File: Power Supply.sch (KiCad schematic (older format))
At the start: 24 parts

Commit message: Added all submoduels
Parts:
- added D?: LED, symbol LED
- added SW?: SPST, symbol SPST
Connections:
- net Earth: no longer R?.2
- net GND: now also D?.2 (A)
- net at D?.2, P?.2 (P2), SW?.1: now also R?.2
- net at F?.2, SW?.5: now also SW?.1
- net at D?.2 (A): now also D?.1 (K); no longer R?.1
- new net Voltage Multiplier/VAC+: SW?.2
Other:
- moved on the sheet: R?
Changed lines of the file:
@@
 LIBS:contrib
 LIBS:valves
-LIBS:switch_dpdt
-LIBS:switch_spdt
 LIBS:Power Supply-cache
 EELAYER 25 0
@@
 $Descr A4 11693 8268
 encoding utf-8
-Sheet 1 1
+Sheet 1 5
 Title "Power Supply"
 Date ""
@@
 L R R?
 U 1 1 55CE60EE
-P 4450 4650
-F 0 "R?" V 4530 4650 50  0000 C CNN
-F 1 "R" V 4450 4650 50  0000 C CNN
-F 2 "" V 4380 4650 30  0000 C CNN
-F 3 "" H 4450 4650 30  0000 C CNN
-	1    4450 4650
-	1    0    0    -1
-$EndComp
-$Comp
-L Earth #PWR?
-U 1 1 55CE6153
-P 4450 4800
-F 0 "#PWR?" H 4450 4550 50  0001 C CNN
-F 1 "Earth" H 4450 4650 50  0001 C CNN
-F 2 "" H 4450 4800 60  0000 C CNN
-F 3 "" H 4450 4800 60  0000 C CNN
-	1    4450 4800
+P 4600 4650
+F 0 "R?" V 4680 4650 50  0000 C CNN
+F 1 "R" V 4600 4650 50  0000 C CNN
+F 2 "" V 4530 4650 30  0000 C CNN
+F 3 "" H 4600 4650 30  0000 C CNN
+	1    4600 4650
 	1    0    0    -1
 $EndComp
@@
 	1    0    0    -1
 $EndComp
+$Sheet
+S 5400 900  1400 1450
+U 564515C4
+F0 "Voltage Multiplier" 60
+F1 "Voltage Multiplier.sch" 60
+F2 "VAC+" I L 5400 1200 60
+F3 "VAC-" I L 5400 1950 60
+F4 "5xVDC" I R 6800 1950 60
+$EndSheet
+$Sheet
+S 9400 4200 1200 1450
+U 564650FF
+F0 "Timer" 60
+F1 "Timer.sch" 60
+$EndSheet
+$Sheet
+S 8250 900  1150 1500
+U 56465396
+F0 "Signal Amplifier" 60
+F1 "Signal Amplifier.sch" 60
+$EndSheet
+$Comp
+L Earth #PWR?
+U 1 1 56468113
+P 5200 2000
+F 0 "#PWR?" H 5200 1750 50  0001 C CNN
+F 1 "Earth" H 5200 1850 50  0001 C CNN
+F 2 "" H 5200 2000 60  0000 C CNN
+F 3 "" H 5200 2000 60  0000 C CNN
+	1    5200 2000
+	1    0    0    -1
+$EndComp
+$Comp
+L LED D?
+U 1 1 5646910E
+P 4750 4300
+F 0 "D?" H 4750 4400 50  0000 C CNN
+F 1 "LED" H 4750 4200 50  0000 C CNN
+F 2 "" H 4750 4300 60  0000 C CNN
+F 3 "" H 4750 4300 60  0000 C CNN
+	1    4750 4300
+	0    -1   -1   0
+$EndComp
 Wire Wire Line
 	3800 2100 4100 2100
@@
 	2600 2800 2600 2600
 Wire Wire Line
-	2600 2100 2600 2000
+	2600 1200 2600 2100
 Wire Wire Line
 	2600 2000 2800 2000
@@
 	2600 3700 4100 3700
 Wire Wire Line
-	4100 3700 4100 3600
+	4100 3600 4100 4900
 Wire Wire Line
 	2400 3100 2400 3000
@@
 	6050 2900 6050 3050
 Wire Wire Line
-	5650 3350 5650 3900
+	5650 3900 5650 3350
 Wire Wire Line
 	6050 3900 6050 3350
@@
 	3250 4400 2850 4400
 Connection ~ 3250 3900
-Wire Wire Line
-	4450 4100 4450 3900
-Connection ~ 4450 3900
 Wire Wire Line
 	7750 2900 7750 3200
@@
 Connection ~ 5650 3900
 Connection ~ 5650 2900
+Wire Wire Line
+	5200 2000 5200 1950
+Wire Wire Line
+	5200 1950 5400 1950
+Wire Wire Line
+	4750 4500 4450 4500
+Wire Wire Line
+	4450 4100 4750 4100
+Wire Wire Line
+	4600 4800 4600 4900
+Wire Wire Line
+	4600 4900 4100 4900
+Connection ~ 4100 3700
+Wire Wire Line
+	4600 4100 4600 3900
+Connection ~ 4600 3900
+Connection ~ 4600 4100
+$Sheet
+S 6800 4500 1200 1600
+U 5646AC7D
+F0 "Variable Regulators" 60
+F1 "Variable Regulators.sch" 60
+$EndSheet
+$Comp
+L SPST SW?
+U 1 1 5646B61A
+P 4900 1200
+F 0 "SW?" H 4900 1300 50  0000 C CNN
+F 1 "SPST" H 4900 1100 50  0000 C CNN
+F 2 "" H 4900 1200 60  0000 C CNN
+F 3 "" H 4900 1200 60  0000 C CNN
+	1    4900 1200
+	1    0    0    -1
+$EndComp
+Wire Wire Line
+	4400 1200 2600 1200
+Connection ~ 2600 2000
 $EndSCHEMATC

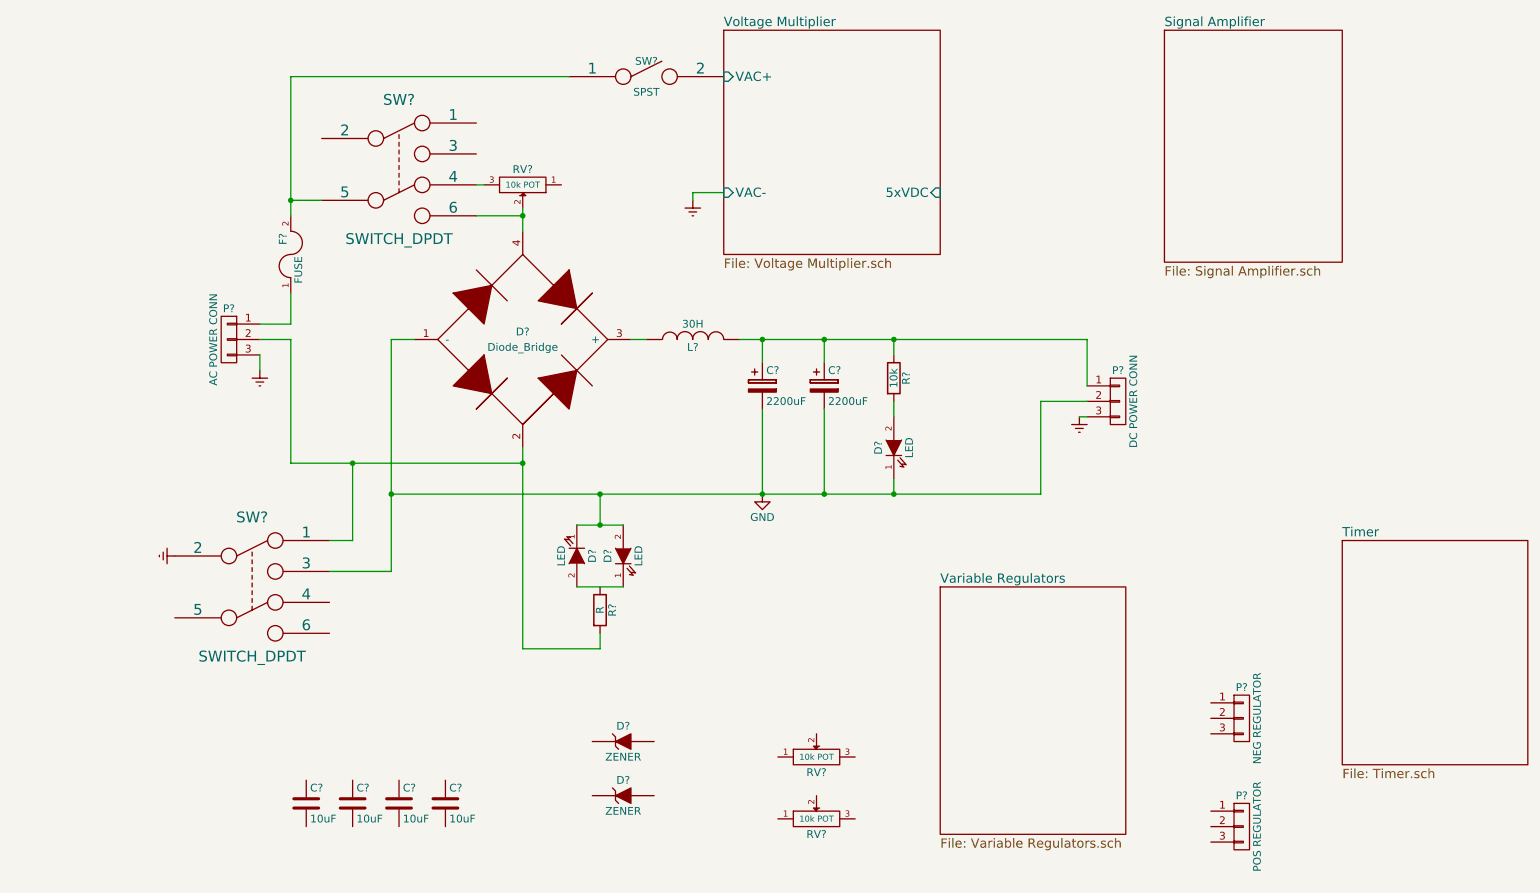
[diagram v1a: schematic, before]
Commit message: Added simulations, Added relays and leak resistors to Voltage multiplier, Created timer circuit...
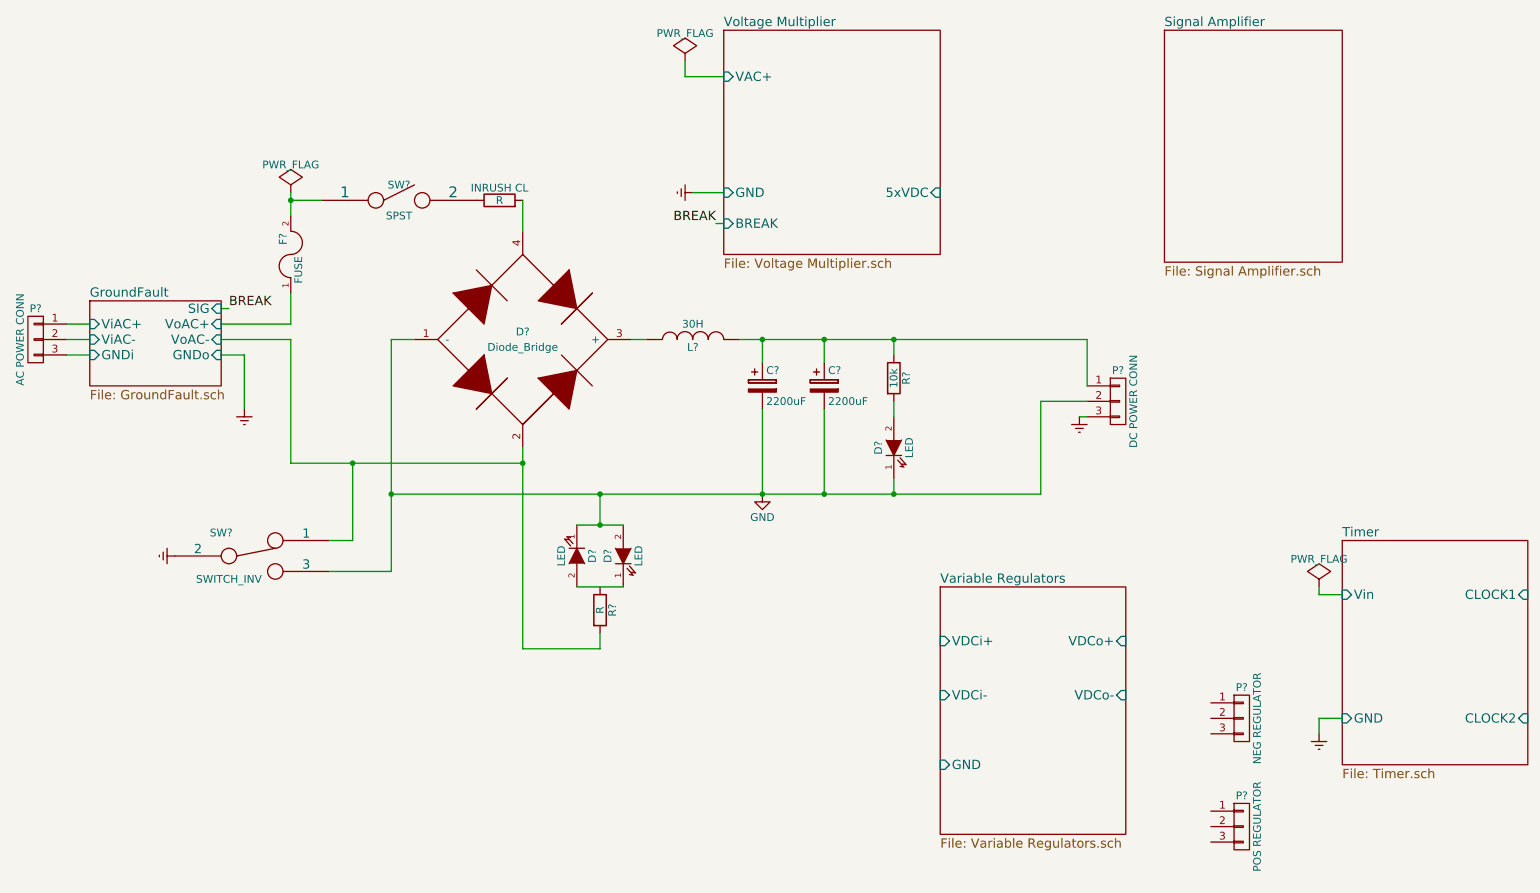
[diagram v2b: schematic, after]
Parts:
- removed C? (x4): 10uF, symbol C
- removed D? (x2): ZENER, symbol ZENER
- removed RV? (x3): 10k POT, symbol POT
- removed SW? (x2): SWITCH_DPDT, symbol SWITCH_DPDT
- removed SW?: SPST, symbol SPST
- added INRUSH~CL: R, symbol R
- added SW?: SPST, symbol SPST
- added SW?: SWITCH_INV, symbol SWITCH_INV
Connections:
- net Earth: now also SW?.2; no longer P?.3 (P3)
- net GND: now also SW?.3
- net GroundFault/VoAC-: now reaches D?.2, R?.2
- net GroundFault/VoAC-: now also SW?.1; no longer P?.2 (P2)
- net at D?.4: now also INRUSH~CL.2
- net GroundFault/ViAC+: now reaches P?.1 (P1)
- net GroundFault/ViAC+: no longer F?.1
- net at F?.2: now also SW?.1
- new net: INRUSH~CL.1, SW?.2
- new net GroundFault/GNDi: P?.3 (P3)
- new net GroundFault/ViAC-: P?.2 (P2)
- new net GroundFault/VoAC+: F?.1
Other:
- moved on the sheet: P?
